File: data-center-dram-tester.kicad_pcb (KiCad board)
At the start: 10 copper layers, 152.9 x 90 mm, 322 parts, among them IC1 TPS54561, IC3 TPD8S009DSMR, J1 0878311420, J10 61300311121, J3 DC_SOCKET, J4 WE_629105150521, J6 685119134923, J7 1140084168, J8 61300311121, Q2 BSS138APW, Q3 BSS138APW, Q4 BSS138APW, Q5 BSS138APW, Q6 BSS138APW, Q7 BSS138APW, Q8 BSS138APW, U10 LM3881MME_NOPB, U11 S27KL0641DABHI023, U12 TPS62823DLCT, U14 2199155-1, U15 XC7K160T-FFG676, U3 S25FL128SAGNFI000, U4 TPS65296, U5 TPS62823DLCT, U6 KSZ9031RNXCA, U7 FT4232HQ, U8 SRST, U9 TPS62823DLCT, Y1 ABM8G-25.000MHZ-18-D2Y-T, Y2 ABM8G-12.000MHZ-18-D2Y-T

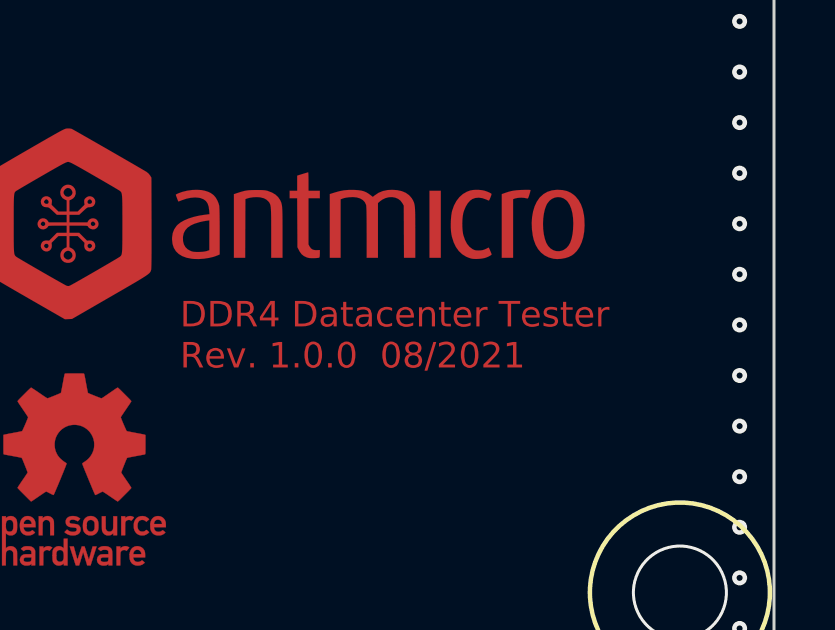
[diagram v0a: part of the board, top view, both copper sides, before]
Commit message: Update naming convention
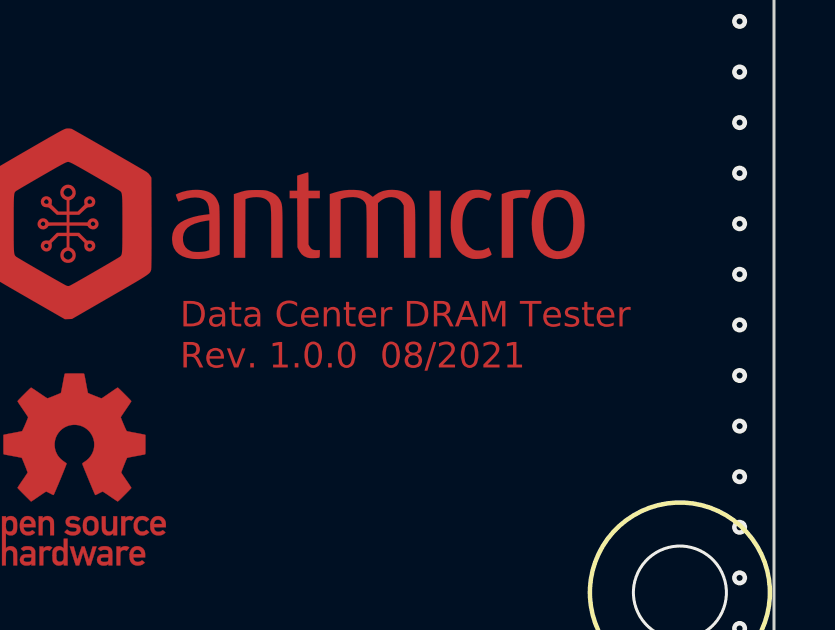
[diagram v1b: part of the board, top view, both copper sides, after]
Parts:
- 0V6, 1V1, 1V8, 3V3, 5V0, PUDC_B1, TP1, TP2, TP3, TP4, TP5, TP6, TP7, TP8, TP9, U8: footprint datacenter-dram-tester-footprints:Testpoint_smd_1mm -> data-center-dram-tester-footprints:Testpoint_smd_1mm
- C1, C10, C100, C102, C109, C180, C182, C183, C2, C27, C28, C29, C31, C33, C37, C39, C4, C40, C41, C42, C45, C97, C98: footprint datacenter-dram-tester-footprints:0603-cap -> data-center-dram-tester-footprints:0603-cap
- C101, C103, C104, C105, C119, C120, C121, C122, C123, C124, C125, C126, C127, C128, C129, C130, C131, C132, C133, C134, C135, C136, C137, C138, C139, C140, C141, C142, C147, C148, C149, C150, C151, C152, C172, C174, C175, C178, C184, C185, C186, C187, C188, C189, C190, C191, C192, C193, C194, C195, C196, C197, C198, C30, C35, C36, C38, C46, C5, C96, C99: footprint datacenter-dram-tester-footprints:0402-cap -> data-center-dram-tester-footprints:0402-cap
- C116, C117, C118: footprint datacenter-dram-tester-footprints:1206-cap -> data-center-dram-tester-footprints:1206-cap
- C20: footprint datacenter-dram-tester-footprints:KEMET_A -> data-center-dram-tester-footprints:KEMET_A
- C26: footprint datacenter-dram-tester-footprints:KEMET_D -> data-center-dram-tester-footprints:KEMET_D
- D1, D10, D5, D6, D7, D8, D9, PWR1: footprint datacenter-dram-tester-footprints:LED_0603 -> data-center-dram-tester-footprints:LED_0603
- D11, D2: footprint datacenter-dram-tester-footprints:PDS760-13 -> data-center-dram-tester-footprints:PDS760-13
- D3: footprint datacenter-dram-tester-footprints:SOT-3 -> data-center-dram-tester-footprints:SOT-3
- D4: footprint datacenter-dram-tester-footprints:TPD6E05U06 -> data-center-dram-tester-footprints:TPD6E05U06
- FB1, FB2, FB3, FB7, R38, R39, R41, R43, R44, R47, R48, R49, R85: footprint datacenter-dram-tester-footprints:0603-res -> data-center-dram-tester-footprints:0603-res
- FB4, FB5, FB6: footprint datacenter-dram-tester-footprints:0603 -> data-center-dram-tester-footprints:0603
- IC1: footprint datacenter-dram-tester-footprints:WSON-10_4x4 -> data-center-dram-tester-footprints:WSON-10_4x4
- IC3: footprint datacenter-dram-tester-footprints:R-PDSO-N15 -> data-center-dram-tester-footprints:R-PDSO-N15
- J1: footprint datacenter-dram-tester-footprints:PinHeader_2x7_P2mm_Drill1mm -> data-center-dram-tester-footprints:PinHeader_2x7_P2mm_Drill1mm
- J10, J8, MODE2: footprint datacenter-dram-tester-footprints:PinHeader_1x3_P2.54_Drill1.1mm -> data-center-dram-tester-footprints:PinHeader_1x3_P2.54_Drill1.1mm
- J3: footprint datacenter-dram-tester-footprints:DC_SOCKET -> data-center-dram-tester-footprints:DC_SOCKET
- J4: footprint datacenter-dram-tester-footprints:USB_Micro_B_Female_629105150521 -> data-center-dram-tester-footprints:USB_Micro_B_Female_629105150521
- J6: footprint datacenter-dram-tester-footprints:HDMI_A_Female_685119134923 -> data-center-dram-tester-footprints:HDMI_A_Female_685119134923
- J7: footprint datacenter-dram-tester-footprints:MicroSD_1140084168 -> data-center-dram-tester-footprints:MicroSD_1140084168
- J?1: footprint datacenter-dram-tester-footprints:7499111121A -> data-center-dram-tester-footprints:7499111121A
- L1: footprint datacenter-dram-tester-footprints:IHLP2020BZER4R7M01 -> data-center-dram-tester-footprints:IHLP2020BZER4R7M01
- L2: footprint datacenter-dram-tester-footprints:INDC3225X120N -> data-center-dram-tester-footprints:INDC3225X120N
- L3, L4, L5: footprint datacenter-dram-tester-footprints:IHLP-1212AE -> data-center-dram-tester-footprints:IHLP-1212AE
- L6: footprint datacenter-dram-tester-footprints:WE_7447798720 -> data-center-dram-tester-footprints:WE_7447798720
- N1: footprint datacenter-dram-tester-footprints:oshw-logo -> data-center-dram-tester-footprints:oshw-logo
- N2: footprint datacenter-dram-tester-footprints:antmicro-logo_scaled_20mm -> data-center-dram-tester-footprints:antmicro-logo_scaled_20mm
- PROG_B1, USR_BTN1, USR_BTN2, USR_BTN3, USR_BTN4: footprint datacenter-dram-tester-footprints:Switch_Tactile_SMD_B3U-1000P -> data-center-dram-tester-footprints:Switch_Tactile_SMD_B3U-1000P
- Q2, Q3, Q4, Q5, Q6, Q7, Q8: footprint datacenter-dram-tester-footprints:SC70-3 -> data-center-dram-tester-footprints:SC70-3
- R1, R10, R11, R115, R116, R119, R12, R122, R126, R127, R128, R129, R13, R130, R131, R132, R133, R134, R135, R136, R137, R138, R139, R14, R140, R141, R142, R143, R144, R145, R146, R15, R16, R17, R18, R19, R2, R20, R21, R22, R23, R24, R25, R26, R27, R28, R29, R3, R30, R31, R32, R33, R34, R35, R36, R37, R4, R40, R42, R45, R5, R50, R51, R52, R53, R54, R55, R56, R57, R58, R59, R6, R60, R61, R62, R67, R68, R69, R7, R70, R71, R72, R73, R74, R75, R76, R77, R78, R79, R8, R80, R81, R82, R83, R84, R86, R87, R88, R89, R9, R90, R91, R92, R93, R94, R95, R96: footprint datacenter-dram-tester-footprints:0402-res -> data-center-dram-tester-footprints:0402-res
- R100, R101, R102, R103, R104, R105, R106, R107, R108, R109, R110, R111, R112, R113, R114, R117, R118, R120, R121, R123, R124, R125, R147, R148, R149, R150, R151, R152, R153, R154, R155, R156, R157, R97, R98, R99: footprint datacenter-dram-tester-footprints:0201-res -> data-center-dram-tester-footprints:0201-res
- R46: footprint datacenter-dram-tester-footprints:0402 -> data-center-dram-tester-footprints:0402
- S1: footprint datacenter-dram-tester-footprints:Switch_Slide_11.6x4mm_EG1218 -> data-center-dram-tester-footprints:Switch_Slide_11.6x4mm_EG1218
- U10: footprint datacenter-dram-tester-footprints:VSSOP8-Texas_Instruments-DGK0008A -> data-center-dram-tester-footprints:VSSOP8-Texas_Instruments-DGK0008A
- U11: footprint datacenter-dram-tester-footprints:FBGA-24 -> data-center-dram-tester-footprints:FBGA-24
- U12, U5, U9: footprint datacenter-dram-tester-footprints:QFN-8_2x1mm -> data-center-dram-tester-footprints:QFN-8_2x1mm
- U14: footprint datacenter-dram-tester-footprints:2199155-1 -> data-center-dram-tester-footprints:2199155-1
- U15: footprint datacenter-dram-tester-footprints:BGA676C100P26X26_2700X2700X254 -> data-center-dram-tester-footprints:BGA676C100P26X26_2700X2700X254
- U3: footprint datacenter-dram-tester-footprints:S25FL128SAGNFI000 -> data-center-dram-tester-footprints:S25FL128SAGNFI000
- U4: footprint datacenter-dram-tester-footprints:VQFN-HR -> data-center-dram-tester-footprints:VQFN-HR
- U6: footprint datacenter-dram-tester-footprints:QFN-48-Microchip-QFN77-48LD-PL-2 -> data-center-dram-tester-footprints:QFN-48-Microchip-QFN77-48LD-PL-2
- U7: footprint datacenter-dram-tester-footprints:FT4232HQ -> data-center-dram-tester-footprints:FT4232HQ
- Y1, Y2: footprint datacenter-dram-tester-footprints:KX-7 -> data-center-dram-tester-footprints:KX-7
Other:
- board text added: "Data Center DRAM Tester Rev. 1.0.0 08/2021"
- board text removed: "DDR4 Datacenter Tester Rev. 1.0.0 08/2021"

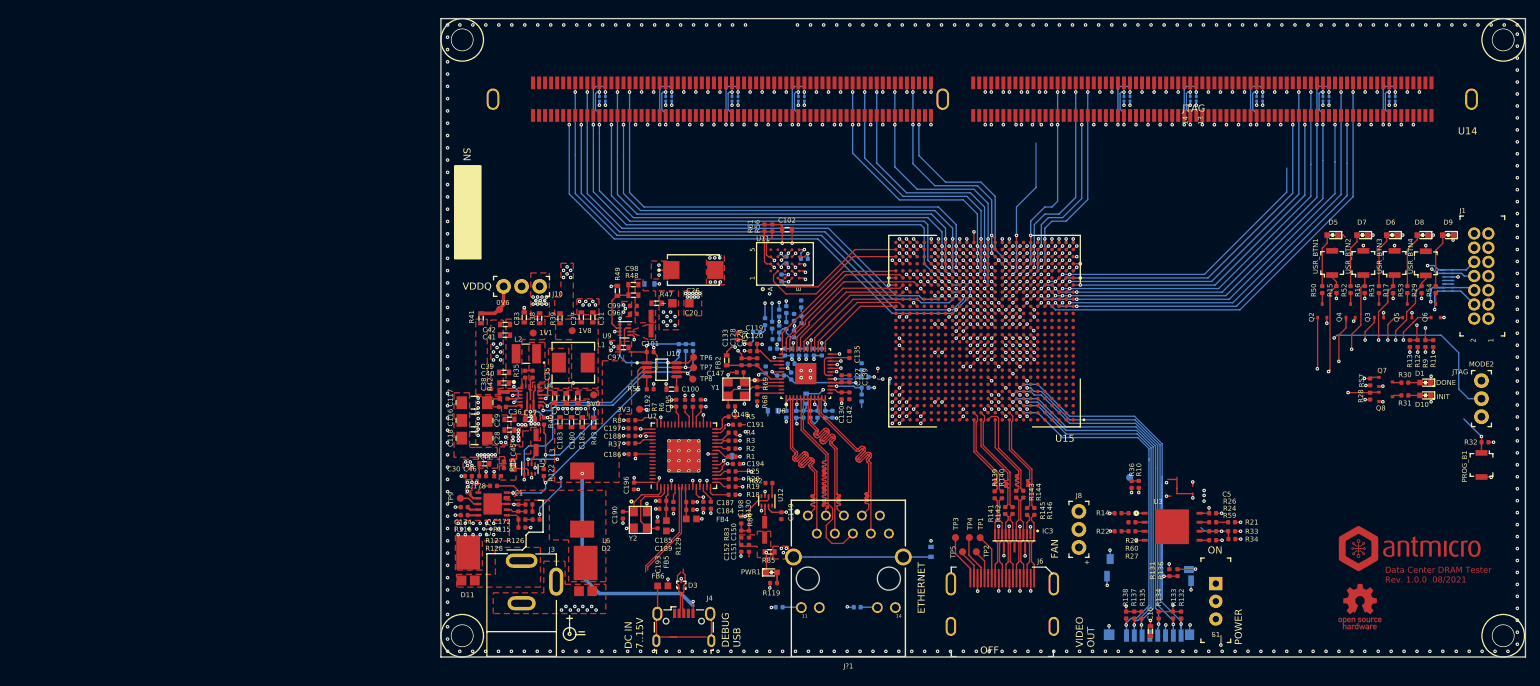
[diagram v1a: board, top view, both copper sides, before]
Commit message: Add Power Supply component placement - WIP
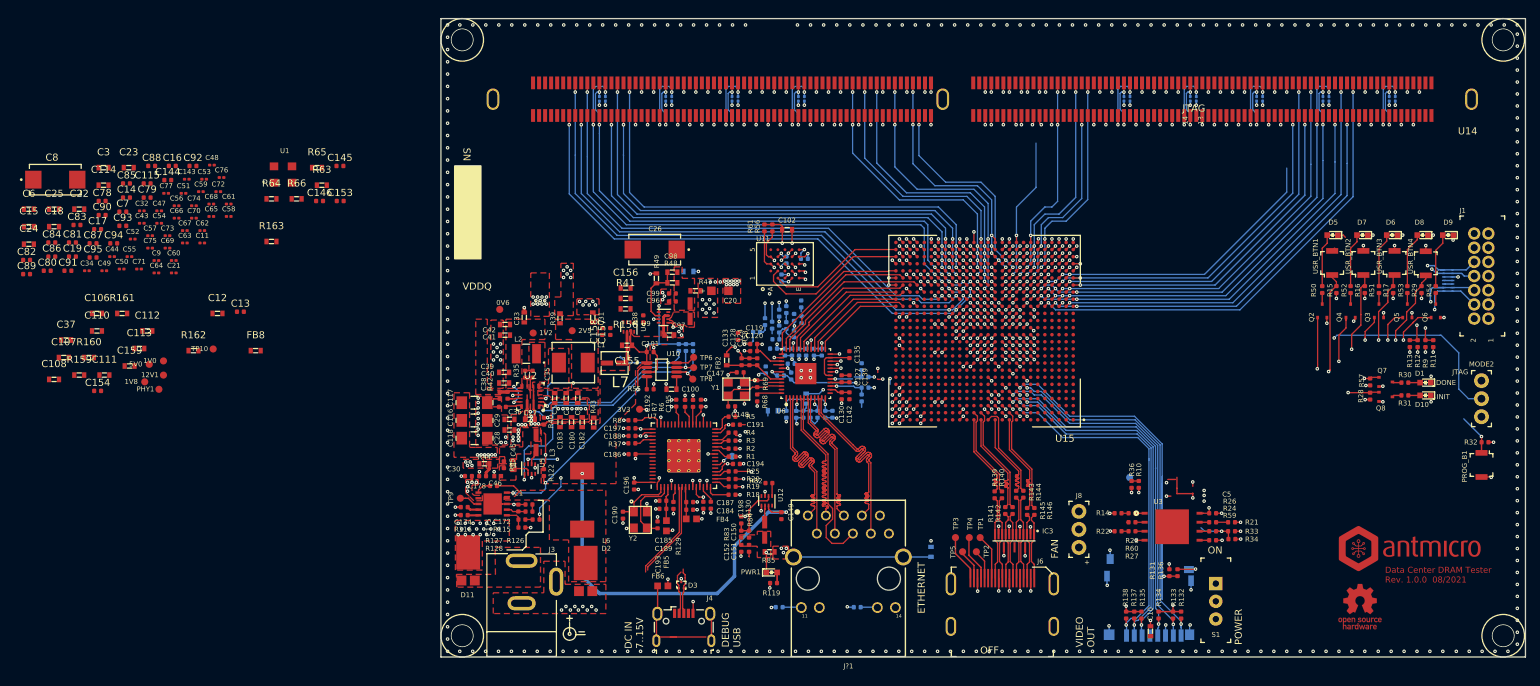
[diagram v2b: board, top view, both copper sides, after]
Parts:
- removed J10: 61300311121, data-center-dram-tester-footprints:PinHeader_1x3_P2.54_Drill1.1mm
- added 12V1: TP_SMD1MM, data-center-dram-tester-footprints:Testpoint_smd_1mm, F.Cu at (67.9, 96.3)
- added 1V0: TP_SMD1MM, data-center-dram-tester-footprints:Testpoint_smd_1mm, F.Cu at (67.9, 94.3)
- added 1V8: TP_SMD1MM, data-center-dram-tester-footprints:Testpoint_smd_1mm, F.Cu at (65.2, 97.3)
- added C106: C_10n_0603, data-center-dram-tester-footprints:0603-cap, F.Cu at (58.5, 87.6)
- added C107: C_10n_0603, data-center-dram-tester-footprints:0603-cap, F.Cu at (53.8, 93.8)
- added C108: C_10n_0603, data-center-dram-tester-footprints:0603-cap, F.Cu at (52.5, 96.9)
- added C11: C_100n_0201, data-center-dram-tester-footprints:0201-res, F.Cu at (73.4, 77.6)
- added C110: C_10n_0603, data-center-dram-tester-footprints:0603-cap, F.Cu at (58.5, 90.0)
- added C111: C_10n_0603, data-center-dram-tester-footprints:0603-cap, F.Cu at (59.6, 96.3)
- added C112: C_10n_0603, data-center-dram-tester-footprints:0603-cap, F.Cu at (65.6, 90.0)
- added C113: C_10n_0603, data-center-dram-tester-footprints:0603-cap, F.Cu at (64.5, 92.5)
- added C114: C_47u_0603, data-center-dram-tester-footprints:0603-cap, F.Cu at (59.4, 69.5)
- added C115: C_4u7_0402, data-center-dram-tester-footprints:0402-cap, F.Cu at (65.6, 69.2)
- added C12: C_47u_0603, data-center-dram-tester-footprints:0603-cap, F.Cu at (75.5, 87.6)
- added C13: C_470n_0402, data-center-dram-tester-footprints:0402-cap, F.Cu at (78.7, 87.3)
- added C14: C_4u7_0402, data-center-dram-tester-footprints:0402-cap, F.Cu at (62.7, 71.2)
- added C143: C_100n_0201, data-center-dram-tester-footprints:0201-res, F.Cu at (71.2, 68.6)
- added C144: C_4u7_0402, data-center-dram-tester-footprints:0402-cap, F.Cu at (68.5, 68.8)
- added C145: C_100n_0402_6V3, data-center-dram-tester-footprints:0402-cap, F.Cu at (92.8, 66.8)
- added C146: C_100n_0402_6V3, data-center-dram-tester-footprints:0402-cap, F.Cu at (89.9, 71.7)
- added C15: C_47u_0603, data-center-dram-tester-footprints:0603-cap, F.Cu at (48.9, 75.3)
- added C153: C_100n_0402_6V3, data-center-dram-tester-footprints:0402-cap, F.Cu at (92.8, 71.7)
- added C154: C_100n_0402_16V, data-center-dram-tester-footprints:0402-cap, F.Cu at (58.6, 98.5)
- added C155: C_10u_0603, antmicro-footprints:0603-cap, F.Cu at (133.2, 92.1)
- added C156: C_120p_0603, antmicro-footprints:0603-cap, F.Cu at (133.0, 84.0)
- added C157: C_10u_0402, data-center-dram-tester-footprints:0402-cap, F.Cu at (130.9, 90.1)
- added C158: C_10u_0402, data-center-dram-tester-footprints:0402-cap, F.Cu at (129.7, 90.1)
- added C159: C_22u_0603, data-center-dram-tester-footprints:0603-cap, F.Cu at (63.1, 95.0)
- added C16: C_4u7_0402, data-center-dram-tester-footprints:0402-cap, F.Cu at (69.1, 66.8)
- added C17: C_4u7_0402, data-center-dram-tester-footprints:0402-cap, F.Cu at (58.6, 75.7)
- added C18: C_47u_0603, data-center-dram-tester-footprints:0603-cap, F.Cu at (52.5, 75.3)
- added C19: C_4u7_0402, data-center-dram-tester-footprints:0402-cap, F.Cu at (55.1, 79.6)
- added C21: C_100n_0201, data-center-dram-tester-footprints:0201-res, F.Cu at (69.3, 81.9)
- added C22: C_47u_0603, data-center-dram-tester-footprints:0603-cap, F.Cu at (56.0, 72.9)
- added C23: C_47u_0603, data-center-dram-tester-footprints:0603-cap, F.Cu at (63.0, 67.0)
- added C24: C_47u_0603, data-center-dram-tester-footprints:0603-cap, F.Cu at (48.9, 77.8)
- added C25: C_47u_0603, data-center-dram-tester-footprints:0603-cap, F.Cu at (52.5, 72.9)
- added C3: C_47u_0603, data-center-dram-tester-footprints:0603-cap, F.Cu at (59.4, 67.0)
- added C32: C_100n_0201, data-center-dram-tester-footprints:0201-res, F.Cu at (64.8, 73.1)
- added C34: C_100n_0201, data-center-dram-tester-footprints:0201-res, F.Cu at (57.1, 81.5)
- added C43: C_100n_0201, data-center-dram-tester-footprints:0201-res, F.Cu at (64.8, 74.9)
- added C44: C_100n_0201, data-center-dram-tester-footprints:0201-res, F.Cu at (60.6, 79.6)
- added C47: C_100n_0201, data-center-dram-tester-footprints:0201-res, F.Cu at (67.3, 73.1)
- added C48: C_100n_0201, data-center-dram-tester-footprints:0201-res, F.Cu at (74.7, 66.7)
- added C49: C_100n_0201, data-center-dram-tester-footprints:0201-res, F.Cu at (59.5, 81.5)
- added C50: C_100n_0201, data-center-dram-tester-footprints:0201-res, F.Cu at (62.0, 81.3)
- added C51: C_100n_0201, data-center-dram-tester-footprints:0201-res, F.Cu at (70.7, 70.6)
- added C52: C_100n_0201, data-center-dram-tester-footprints:0201-res, F.Cu at (63.6, 77.1)
- added C53: C_100n_0201, data-center-dram-tester-footprints:0201-res, F.Cu at (73.6, 68.6)
- added C54: C_100n_0201, data-center-dram-tester-footprints:0201-res, F.Cu at (67.3, 74.9)
- added C55: C_100n_0201, data-center-dram-tester-footprints:0201-res, F.Cu at (63.1, 79.6)
- added C56: C_100n_0201, data-center-dram-tester-footprints:0201-res, F.Cu at (69.7, 72.4)
- added C57: C_100n_0201, data-center-dram-tester-footprints:0201-res, F.Cu at (66.0, 76.6)
- added C58: C_100n_0201, data-center-dram-tester-footprints:0201-res, F.Cu at (77.1, 73.9)
- added C59: C_100n_0201, data-center-dram-tester-footprints:0201-res, F.Cu at (73.2, 70.4)
- added C6: C_47u_0603, data-center-dram-tester-footprints:0603-cap, F.Cu at (48.9, 72.9)
- added C60: C_100n_0201, data-center-dram-tester-footprints:0201-res, F.Cu at (69.3, 80.1)
- added C61: C_100n_0201, data-center-dram-tester-footprints:0201-res, F.Cu at (77.1, 72.1)
- added C62: C_100n_0201, data-center-dram-tester-footprints:0201-res, F.Cu at (73.4, 75.9)
- added C63: C_100n_0201, data-center-dram-tester-footprints:0201-res, F.Cu at (70.9, 77.6)
- added C64: C_100n_0201, data-center-dram-tester-footprints:0201-res, F.Cu at (66.9, 81.9)
- added C65: C_100n_0201, data-center-dram-tester-footprints:0201-res, F.Cu at (74.6, 73.9)
- added C66: C_100n_0201, data-center-dram-tester-footprints:0201-res, F.Cu at (69.7, 74.1)
- added C67: C_100n_0201, data-center-dram-tester-footprints:0201-res, F.Cu at (70.9, 75.9)
- added C68: C_100n_0201, data-center-dram-tester-footprints:0201-res, F.Cu at (74.6, 72.1)
- added C69: C_100n_0201, data-center-dram-tester-footprints:0201-res, F.Cu at (68.5, 78.4)
- added C7: C_4u7_0402, data-center-dram-tester-footprints:0402-cap, F.Cu at (62.2, 73.2)
- added C70: C_100n_0201, data-center-dram-tester-footprints:0201-res, F.Cu at (72.2, 74.1)
- added C71: C_100n_0201, data-center-dram-tester-footprints:0201-res, F.Cu at (64.4, 81.3)
- added C72: C_100n_0201, data-center-dram-tester-footprints:0201-res, F.Cu at (75.6, 70.4)
- added C73: C_100n_0201, data-center-dram-tester-footprints:0201-res, F.Cu at (68.5, 76.6)
- added C74: C_100n_0201, data-center-dram-tester-footprints:0201-res, F.Cu at (72.2, 72.4)
- added C75: C_100n_0201, data-center-dram-tester-footprints:0201-res, F.Cu at (66.0, 78.4)
- added C76: C_100n_0201, data-center-dram-tester-footprints:0201-res, F.Cu at (76.1, 68.4)
- added C77: C_100n_0201, data-center-dram-tester-footprints:0201-res, F.Cu at (68.3, 70.6)
- added C78: C_4u7_0402, data-center-dram-tester-footprints:0402-cap, F.Cu at (59.2, 71.7)
- added C79: C_4u7_0402, data-center-dram-tester-footprints:0402-cap, F.Cu at (65.6, 71.2)
- added C8: C_330u_KEMET_D, data-center-dram-tester-footprints:KEMET_D, F.Cu at (52.6, 68.7)
- added C80: C_4u7_0402, data-center-dram-tester-footprints:0402-cap, F.Cu at (51.5, 81.5)
- added C81: C_4u7_0402, data-center-dram-tester-footprints:0402-cap, F.Cu at (55.1, 77.6)
- added C82: C_4u7_0402, data-center-dram-tester-footprints:0402-cap, F.Cu at (48.6, 80.0)
- added C83: C_4u7_0402, data-center-dram-tester-footprints:0402-cap, F.Cu at (55.7, 75.1)
- added C84: C_4u7_0402, data-center-dram-tester-footprints:0402-cap, F.Cu at (52.1, 77.6)
- added C85: C_4u7_0402, data-center-dram-tester-footprints:0402-cap, F.Cu at (62.7, 69.2)
- added C86: C_4u7_0402, data-center-dram-tester-footprints:0402-cap, F.Cu at (52.1, 79.6)
- added C87: C_4u7_0402, data-center-dram-tester-footprints:0402-cap, F.Cu at (58.0, 77.7)
- added C88: C_4u7_0402, data-center-dram-tester-footprints:0402-cap, F.Cu at (66.2, 66.8)
- added C89: C_4u7_0402, data-center-dram-tester-footprints:0402-cap, F.Cu at (48.6, 82.0)
- added C9: C_100n_0201, data-center-dram-tester-footprints:0201-res, F.Cu at (66.9, 80.1)
- added C90: C_4u7_0402, data-center-dram-tester-footprints:0402-cap, F.Cu at (59.2, 73.7)
- added C91: C_4u7_0402, data-center-dram-tester-footprints:0402-cap, F.Cu at (54.4, 81.5)
- added C92: C_4u7_0402, data-center-dram-tester-footprints:0402-cap, F.Cu at (72.0, 66.8)
- added C93: C_4u7_0402, data-center-dram-tester-footprints:0402-cap, F.Cu at (62.2, 75.2)
- added C94: C_4u7_0402, data-center-dram-tester-footprints:0402-cap, F.Cu at (60.9, 77.7)
- added C95: C_4u7_0402, data-center-dram-tester-footprints:0402-cap, F.Cu at (58.0, 79.7)
- added FB8: BLM18PG121SN1D, data-center-dram-tester-footprints:0603-res, F.Cu at (80.9, 92.8)
- added L7: IHLP1212AEERR47M11, data-center-dram-tester-footprints:IHLP-1212AE, F.Cu at (131.5, 94.6)
- added PHY1: TP_SMD1MM, data-center-dram-tester-footprints:Testpoint_smd_1mm, F.Cu at (67.2, 98.3)
- added R156: R_100k_0603, antmicro-footprints:0603-res, F.Cu at (133.0, 86.9)
- added R159: R_0R_0603, data-center-dram-tester-footprints:0603-res, F.Cu at (56.0, 96.3)
- added R160: R_0R_0603, data-center-dram-tester-footprints:0603-res, F.Cu at (57.4, 93.8)
- added R161: R_0R_0603, data-center-dram-tester-footprints:0603-res, F.Cu at (62.1, 87.6)
- added R162: R_0R_0603, antmicro-footprints:0603-res, F.Cu at (72.1, 92.8)
- added R163: R_0R_0603, data-center-dram-tester-footprints:0603-res, F.Cu at (83.1, 77.4)
- added R63: R_120R_0603, data-center-dram-tester-footprints:0603-res, F.Cu at (90.2, 69.5)
- added R64: R_120R_0603, data-center-dram-tester-footprints:0603-res, F.Cu at (83.1, 71.4)
- added R65: R_1k_0603, data-center-dram-tester-footprints:0603-res, F.Cu at (89.5, 67.0)
- added R66: R_1k_0603, data-center-dram-tester-footprints:0603-res, F.Cu at (86.7, 71.4)
- added TP10: TP_SMD1MM, antmicro-footprints:Testpoint_smd_1mm, F.Cu at (74.9, 92.6)
- added U1: ASFLMB-100.000MHZ-XY-T, data-center-dram-tester-footprints:ASFLMB-100.000MHZ-XY-T, F.Cu at (84.7, 68.0)
- added U2: TPS65295RJET, antmicro-footprints:TPS65295RJET, F.Cu at (119.6, 99.3)
- C37: value C_22u_0603 -> C_10u_25V_0603
- R38: value R_0R_0603 -> R_0R_0402; footprint data-center-dram-tester-footprints:0603-res -> data-center-dram-tester-footprints:0402-res
- R41: value R_0R_0603 -> R_49R9_0603; footprint data-center-dram-tester-footprints:0603-res -> antmicro-footprints:0603-res
- U4: value TPS65296 -> TPS62823DLCT; footprint data-center-dram-tester-footprints:VQFN-HR -> data-center-dram-tester-footprints:QFN-8_2x1mm
- moved C37 72.7 mm to (54.2, 91.3), turned to 0 degrees
- moved 5V0 62.8 mm to (65.9, 94.8), turned to 0 degrees
- moved R41 20.6 mm to (133.0, 85.5), turned to 0 degrees
- moved U4 17.8 mm to (133.5, 89.5), turned to 270 degrees
- moved R38 14.6 mm to (135.5, 88.3)
- moved C97 6.67 mm to (139.2, 90.6), turned to 0 degrees
- moved C26 6.16 mm to (137.1, 78.6), turned to 180 degrees
- moved C109 5.77 mm to (141.9, 81.6)
- moved C20 5.77 mm to (145.1, 84.4)
- moved C96 5.77 mm to (139.6, 85.9)
- moved C98 5.77 mm to (139.6, 81.8)
- moved C99 5.77 mm to (139.6, 84.8)
- moved L4 5.77 mm to (142.1, 87.2)
- moved R47 5.77 mm to (142.9, 84.4)
- moved R48 5.77 mm to (139.6, 83.2)
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- renumbered 1V1 to 1V2, 1V8 to 2V5, R156 to R164, R157 to R165
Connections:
- net 12V renamed NC
- net Net-(C96-Pad1) renamed VCC1V0
- 0V6 pad 1: VDD0V6 -> VCC0V6
- 1V2 pad 1: VDD1V1 -> VDD1V2
- 2V5 pad 1: VDD1V8 -> VCC2V5
- 3V3 pad 1: 3V3_SYS -> VCC3V3
- C1 pad 1: VCC5V0 -> 5V0_SYS
- C101 pad 1: VCC5V0_INT -> VCC5V0
- C119 pad 1: VCC1V2 -> 1V2_SYS
- C120 pad 1: VCC1V2 -> 1V2_SYS
- C122 pad 1: VCC1V2 -> 1V2_SYS
- C126 pad 1: VCC1V2 -> 1V2_SYS
- C130 pad 1: VCC1V2 -> 1V2_SYS
- C135 pad 1: VCC1V2 -> 1V2_SYS
- C138 pad 1: VCC1V2 -> 1V2_SYS
- C141 pad 1: VCC1V2 -> 1V2_SYS
- C142 pad 1: VCC1V2 -> 1V2_SYS
- C149 pad 1: VCC5V0_INT -> VCC5V0
- C150 pad 1: Net-(C150-Pad1) -> VCC1V2
- C151 pad 1: Net-(C150-Pad1) -> VCC1V2
- C152 pad 1: Net-(C150-Pad1) -> VCC1V2
- C180 pad 1: VCC5V0_INT -> VCC5V0
- C182 pad 1: VCC5V0_INT -> VCC5V0
- C183 pad 1: VCC5V0_INT -> VCC5V0
- C2 pad 1: VCC5V0 -> 5V0_SYS
- C31 pad 1: VDD1V8 -> VCC2V5
- C33 pad 1: VDD1V1 -> VDDQ
- C36 pad 1: Net-(C36-Pad1) -> /Supply/VTTREF
- C37 pad 1: VDD1V8 -> 5V0_SYS
- C38 pad 1: Net-(C38-Pad1) -> VCC0V6
- C39 pad 1: VDD1V1 -> VDD1V2
- C4 pad 1: VCC5V0 -> 5V0_SYS
- C40 pad 1: VDD1V1 -> VDD1V2
- C41 pad 1: VDD1V1 -> VDD1V2
- C42 pad 1: VDD1V1 -> VDD1V2
- C45 pad 1: Net-(C45-Pad1) -> VCC3V3
- C46 pad 1: 3V3_SYS -> VCC3V3
- C97 pad 1: VCC5V0_INT -> VCC5V0
- FB2 pad 2: VCC1V2 -> 1V2_SYS
- FB3 pad 2: VCC1V2 -> 1V2_SYS
- J8 pad 1: VCC5V0_INT -> VCC5V0
- L1 pad 2: VDD1V8 -> VCC2V5
- L2 pad 2: VDD1V1 -> VDD1V2
- L3 pad 2: Net-(C45-Pad1) -> VCC3V3
- L5 pad 2: Net-(C150-Pad1) -> VCC1V2
- L6 pad 2: VCC5V0_INT -> VCC5V0
- R126 pad 1: VCC5V0_INT -> VCC5V0
- R38 pad 1: VDD1V1 -> Net-(R38-Pad1)
- R38 pad 2: 1V1_SYS -> /Supply/VCC_AUX_EN
- R39 pad 1: VDD1V8 -> VCC1V8
- R40 pad 2: VCC5V0 -> 5V0_SYS
- R41 pad 1: Net-(C38-Pad1) -> VCC1V8
- R41 pad 2: VDD0V6 -> Net-(C156-Pad2)
- R42 pad 2: Net-(C38-Pad1) -> VCC0V6
- R43 pad 2: VCC5V0_INT -> 5V0_SYS
- R44 pad 2: Net-(C45-Pad1) -> VCC3V3
- R45 pad 1: Net-(C45-Pad1) -> VCC3V3
- R83 pad 1: Net-(C150-Pad1) -> VCC1V2
- R85 pad 2: Net-(C150-Pad1) -> 1V2_SYS
- R86 pad 1: VCC5V0_INT -> VCC5V0
- R87 pad 1: VCC5V0_INT -> VCC5V0
- R88 pad 1: VCC5V0_INT -> VCC5V0
- U10 pad 1: VCC5V0_INT -> VCC5V0
- U12 pad 7: VCC5V0_INT -> VCC5V0
- U14 pad 101: VSS -> GND
- U14 pad 103: VSS -> GND
- U14 pad 105: VSS -> GND
- U14 pad 107: VSS -> GND
- U14 pad 109: VSS -> GND
- U14 pad 11: VSS -> GND
- U14 pad 112: VSS -> GND
- U14 pad 114: VSS -> GND
- U14 pad 116: VSS -> GND
- U14 pad 118: VSS -> GND
- U14 pad 120: VSS -> GND
- U14 pad 123: VSS -> GND
- U14 pad 125: VSS -> GND
- U14 pad 127: VSS -> GND
- U14 pad 129: VSS -> GND
- U14 pad 13: VSS -> GND
- U14 pad 131: VSS -> GND
- U14 pad 134: VSS -> GND
- U14 pad 136: VSS -> GND
- U14 pad 138: VSS -> GND
- U14 pad 147: VSS -> GND
- U14 pad 149: VSS -> GND
- U14 pad 15: VSS -> GND
- U14 pad 151: VSS -> GND
- U14 pad 154: VSS -> GND
- U14 pad 156: VSS -> GND
- U14 pad 158: VSS -> GND
- U14 pad 160: VSS -> GND
- U14 pad 162: VSS -> GND
- U14 pad 165: VSS -> GND
- U14 pad 167: VSS -> GND
- U14 pad 169: VSS -> GND
- U14 pad 17: VSS -> GND
- U14 pad 171: VSS -> GND
- U14 pad 173: VSS -> GND
- U14 pad 176: VSS -> GND
- U14 pad 178: VSS -> GND
- U14 pad 180: VSS -> GND
- U14 pad 182: VSS -> GND
- U14 pad 184: VSS -> GND
- U14 pad 187: VSS -> GND
- U14 pad 189: VSS -> GND
- U14 pad 191: VSS -> GND
- U14 pad 193: VSS -> GND
- U14 pad 195: VSS -> GND
- U14 pad 198: VSS -> GND
- U14 pad 2: VSS -> GND
- U14 pad 20: VSS -> GND
- U14 pad 200: VSS -> GND
- U14 pad 202: VSS -> GND
- U14 pad 204: VSS -> GND
- U14 pad 206: VSS -> GND
- U14 pad 209: VSS -> GND
- U14 pad 212: VSS -> GND
- U14 pad 215: VSS -> GND
- U14 pad 217: VSS -> GND
- U14 pad 22: VSS -> GND
- U14 pad 220: VSS -> GND
- U14 pad 223: VDD -> VDDQ
- U14 pad 226: VDD -> VDDQ
- U14 pad 229: VDD -> VDDQ
- U14 pad 231: VDD -> VDDQ
- U14 pad 233: VDD -> VDDQ
- U14 pad 236: VDD -> VDDQ
- U14 pad 239: VSS -> GND
- U14 pad 24: VSS -> GND
- U14 pad 241: VSS -> GND
- U14 pad 243: VSS -> GND
- U14 pad 246: VSS -> GND
- U14 pad 248: VSS -> GND
- U14 pad 250: VSS -> GND
- U14 pad 252: VSS -> GND
- U14 pad 254: VSS -> GND
- U14 pad 257: VSS -> GND
- U14 pad 259: VSS -> GND
- U14 pad 26: VSS -> GND
- U14 pad 261: VSS -> GND
- U14 pad 263: VSS -> GND
- U14 pad 265: VSS -> GND
- U14 pad 268: VSS -> GND
- U14 pad 270: VSS -> GND
- U14 pad 272: VSS -> GND
- U14 pad 274: VSS -> GND
- U14 pad 276: VSS -> GND
- U14 pad 279: VSS -> GND
- U14 pad 28: VSS -> GND
- U14 pad 281: VSS -> GND
- U14 pad 283: VSS -> GND
- U14 pad 31: VSS -> GND
- U14 pad 33: VSS -> GND
- U14 pad 35: VSS -> GND
- U14 pad 37: VSS -> GND
- U14 pad 39: VSS -> GND
- U14 pad 4: VSS -> GND
- U14 pad 42: VSS -> GND
- U14 pad 44: VSS -> GND
- U14 pad 46: VSS -> GND
- U14 pad 48: VSS -> GND
- U14 pad 50: VSS -> GND
- U14 pad 53: VSS -> GND
- U14 pad 55: VSS -> GND
- U14 pad 57: VSS -> GND
- U14 pad 59: VDD -> VDDQ
- U14 pad 6: VSS -> GND
- U14 pad 61: VDD -> VDDQ
- U14 pad 64: VDD -> VDDQ
- U14 pad 67: VDD -> VDDQ
- U14 pad 70: VDD -> VDDQ
- U14 pad 73: VDD -> VDDQ
- U14 pad 76: VDD -> VDDQ
- U14 pad 80: VDD -> VDDQ
- U14 pad 83: VDD -> VDDQ
- U14 pad 85: VDD -> VDDQ
- U14 pad 88: VDD -> VDDQ
- U14 pad 9: VSS -> GND
- U14 pad 90: VDD -> VDDQ
- U14 pad 92: VDD -> VDDQ
- U14 pad 94: VSS -> GND
- U14 pad 96: VSS -> GND
- U14 pad 98: VSS -> GND
- U4 pad 1: VDD1V1 -> Net-(R38-Pad1)
- U4 pad 2: Net-(C38-Pad1) -> Net-(C156-Pad2)
- U4 pad 4: Net-(R42-Pad1) -> (no net)
- U4 pad 5: VDD1V1 -> GND
- U4 pad 6: Net-(C36-Pad1) -> Net-(L7-Pad1)
- U4 pad 7: VIN -> VCC5V0
- U4 pad 8: Net-(R40-Pad1) -> /Supply/1V8_PG
- U5 pad 7: VCC5V0_INT -> VCC5V0
- U6 pad 14: VCC1V2 -> 1V2_SYS
- U6 pad 18: VCC1V2 -> 1V2_SYS
- U6 pad 23: VCC1V2 -> 1V2_SYS
- U6 pad 26: VCC1V2 -> 1V2_SYS
- U6 pad 30: VCC1V2 -> 1V2_SYS
- U6 pad 39: VCC1V2 -> 1V2_SYS
- U9 pad 7: VCC5V0_INT -> VCC5V0
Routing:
- net VCC5V0: track 18.3 -> 88.8 mm, vias 2 -> 8
- net VCC5V0_INT: track 61.3 -> 0.00 mm, vias 7 -> 0
- net VCC1V2: track 26.1 -> 0.80 mm, vias 12 -> 7
- net 1V2_SYS: track 0.00 -> 25.3 mm, vias 0 -> 5
- net LED_LINK: track 33.5 -> 16.9 mm
- net 5V0_SYS: track 0.00 -> 7.64 mm
- net VDD1V8: track 6.43 -> 0.00 mm, vias 2 -> 0
- net VCC2V5: track 0.00 -> 6.43 mm, vias 0 -> 2
- net VDD0V6: track 6.26 -> 0.00 mm
- net 3V3_SYS: track 107.9 -> 102.5 mm, vias 69 -> 67
- net Net-(L7-Pad1): track 0.00 -> 4.89 mm
- net /Supply/VCC_IO_EN: track 48.5 -> 44.1 mm
- net VDD1V2: track 0.00 -> 3.69 mm, vias 0 -> 2
- net VDD1V1: track 3.69 -> 0.00 mm, vias 2 -> 0
- net VCC0V6: track 0.00 -> 3.14 mm
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- added copper zone on F.Cu, net 5V0_SYS
- added copper zone on F.Cu, net VCC0V6
- added copper zone on F.Cu, net VCC1V8
- added copper zone on F.Cu, net VCC3V3
- added copper zone on F.Cu, net VDD1V2
- removed copper zone on VCC2, net 1V0_SYS
- removed copper zone on VCC2, net 1V1_SYS
- removed copper zone on VCC2, net 1V8_FT
- removed copper zone on VCC2, net 1V8_SYS
- removed copper zone on VCC1, net 3V3_SYS
- removed copper zone on VCC2, net 3V3_SYS
- removed copper zone on VCC1, net GND
- removed copper zone on VCC2, net GND
- removed copper zone on F.Cu, net Net-(C150-Pad1)
- removed copper zone on F.Cu, net Net-(C38-Pad1)
- removed copper zone on F.Cu, net Net-(C45-Pad1)
- removed copper zone on F.Cu, net VCC5V0_INT
- removed copper zone on F.Cu, net VDD1V1
- removed copper zone on F.Cu, net VDD1V8
- removed copper zone on VCC1, net VDDQ

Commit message: Placing capacitors under FPGA - WIP
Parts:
- C32, C34, C43, C44, C50, C52, C54, C57, C58, C59, C60, C61, C62, C63, C64, C65, C66, C67, C68, C69, C70, C71, C77: moved to B.Cu
- moved C34 138.6 mm to (195.6, 78.0), turned to 90 degrees
- moved C71 131.3 mm to (195.8, 81.4), turned to 180 degrees
- moved C50 126.6 mm to (188.1, 91.5), turned to 180 degrees
- moved C52 125.6 mm to (188.2, 92.6), turned to 90 degrees
- moved C54 123.5 mm to (189.2, 94.5), turned to 180 degrees
- moved C77 121.2 mm to (187.1, 94.5), turned to 180 degrees
- moved C44 120.1 mm to (180.8, 80.1), turned to 180 degrees
- moved C32 117.3 mm to (181.7, 82.4), turned to 180 degrees
- moved C69 116.7 mm to (184.2, 93.6), turned to 90 degrees
- moved C43 116.1 mm to (180.1, 88.2), turned to 270 degrees
- moved C57 115.5 mm to (181.1, 86.6), turned to 270 degrees
- moved C66 114.8 mm to (183.2, 91.6), turned to 270 degrees
- moved C64 114.7 mm to (181.2, 91.6), turned to 270 degrees
- moved C67 112.7 mm to (182.2, 93.6), turned to 90 degrees
- moved C63 112.6 mm to (183.2, 86.6), turned to 270 degrees
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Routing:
- net GND: track 181.9 -> 193.0 mm, vias 452 -> 453
- net 1V0_SYS: track 14.1 -> 17.9 mm, vias 29 -> 28
- net VDDQ: track 13.4 -> 15.2 mm
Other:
- net class Default: clearance 0.15 -> 0.1
- rule trace_clearance: 0.15 -> 0.1

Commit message: Add power supply layout - WIP
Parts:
- removed C154: C_100n_0402_16V, data-center-dram-tester-footprints:0402-cap
- removed C37: C_10u_25V_0603, data-center-dram-tester-footprints:0603-cap
- moved TP10 183.3 mm to (255.7, 62.3)
- moved R157 177.9 mm to (247.3, 62.3)
- moved PHY1 83.3 mm to (147.7, 119.7), turned to 90 degrees
- moved R159 68.4 mm to (123.9, 88.2), turned to 90 degrees
- moved FB8 64.9 mm to (145.4, 100.0), turned to 90 degrees
- moved 1V8 64.4 mm to (128.2, 83.8), turned to 90 degrees
- moved C159 53.8 mm to (115.9, 84.7), turned to 180 degrees
- moved R161 50.7 mm to (112.7, 90.5), turned to 90 degrees
- moved R160 43.9 mm to (100.9, 88.0)
- moved R158 42.4 mm to (122.7, 62.5)
- moved 12V1 42.0 mm to (109.9, 97.3), turned to 90 degrees
- moved C108 37.4 mm to (88.7, 87.9)
- moved C107 35.2 mm to (88.7, 89.4)
- moved C110 34.1 mm to (92.4, 86.4)
- moved C111 33.3 mm to (92.4, 90.8)
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- renumbered R162 to R157, R163 to R158, R164 to R162, R165 to R163
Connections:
- C1 pad 1: 5V0_SYS -> Net-(C1-Pad1)
- C33 pad 1: VDDQ -> VDD1V2
- U2 pad 1: VDDQ -> VDD1V2
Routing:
- net Net-(C178-Pad1): track 3.95 -> 16.6 mm
- net 3V3_SYS: track 102.5 -> 93.4 mm, vias 67 -> 65
- net UART0_RX: track 6.76 -> 15.1 mm
- net UART0_TX: track 6.71 -> 15.1 mm
- net LED_SPD: track 35.6 -> 28.2 mm
- net VPP: track 0.00 -> 7.00 mm, vias 0 -> 13
- net UART1_TX: track 19.1 -> 24.1 mm
- net Net-(C156-Pad2): track 0.00 -> 4.83 mm
- net UART1_RX: track 18.8 -> 23.5 mm
- net VDD1V2: track 3.69 -> 7.09 mm, vias 2 -> 16
- net VDDSPD: track 0.00 -> 2.82 mm
- net VTT: track 0.00 -> 2.70 mm, vias 0 -> 16
- net AUX_JTAG_TCK: track 7.51 -> 5.31 mm
- net VCC1V8: track 0.00 -> 2.00 mm
- net Net-(R38-Pad1): track 0.00 -> 1.90 mm
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- added copper zone on F.Cu, net 1V2_SYS
- added copper zone on F.Cu, net VCC2V5
- added copper zone on F.Cu, net VPP
- added copper zone on VCC2, net VPP
- added copper zone on F.Cu, net VTT
- added copper zone on VCC2, net VTT
- removed copper zone on F.Cu, net 1V1_SYS
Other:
- board text removed: "1V1"
